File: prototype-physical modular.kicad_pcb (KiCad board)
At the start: 2 copper layers, 100 x 164 mm, 174 parts, among them CON1 BARREL_JACK, CON2 SD_Card, IC1 ATMEGA2560-A, J1 MIDI_IN, J2 MIDI_OUT, P1 POWER, P15 PH, P16 PF, P17 SD_PINS, P18 3VI2C, P2 FTDI, P3 SPI, P4 BUSTI, P5 BUSTO, P7 PA, Q1 BSS138, Q2 BSS138, Q3 BSS138, Q4 BSS138, Q5 BSS138, Q6 BSS138, SW1 SW_PUSH, SW10 SW_PUSH, SW11 SW_PUSH, SW12 SW_PUSH, SW13 SW_PUSH, SW14 SW_PUSH, SW2 ROTARY_ENCODER_SWITCH, SW3 SW_PUSH, SW4 SW_PUSH, SW5 SW_PUSH, SW6 SW_PUSH, SW7 SW_PUSH, SW8 SW_PUSH, SW9 SW_PUSH, U1 NCP1117ST50T3G, U2 6N138, Y1 16MHz

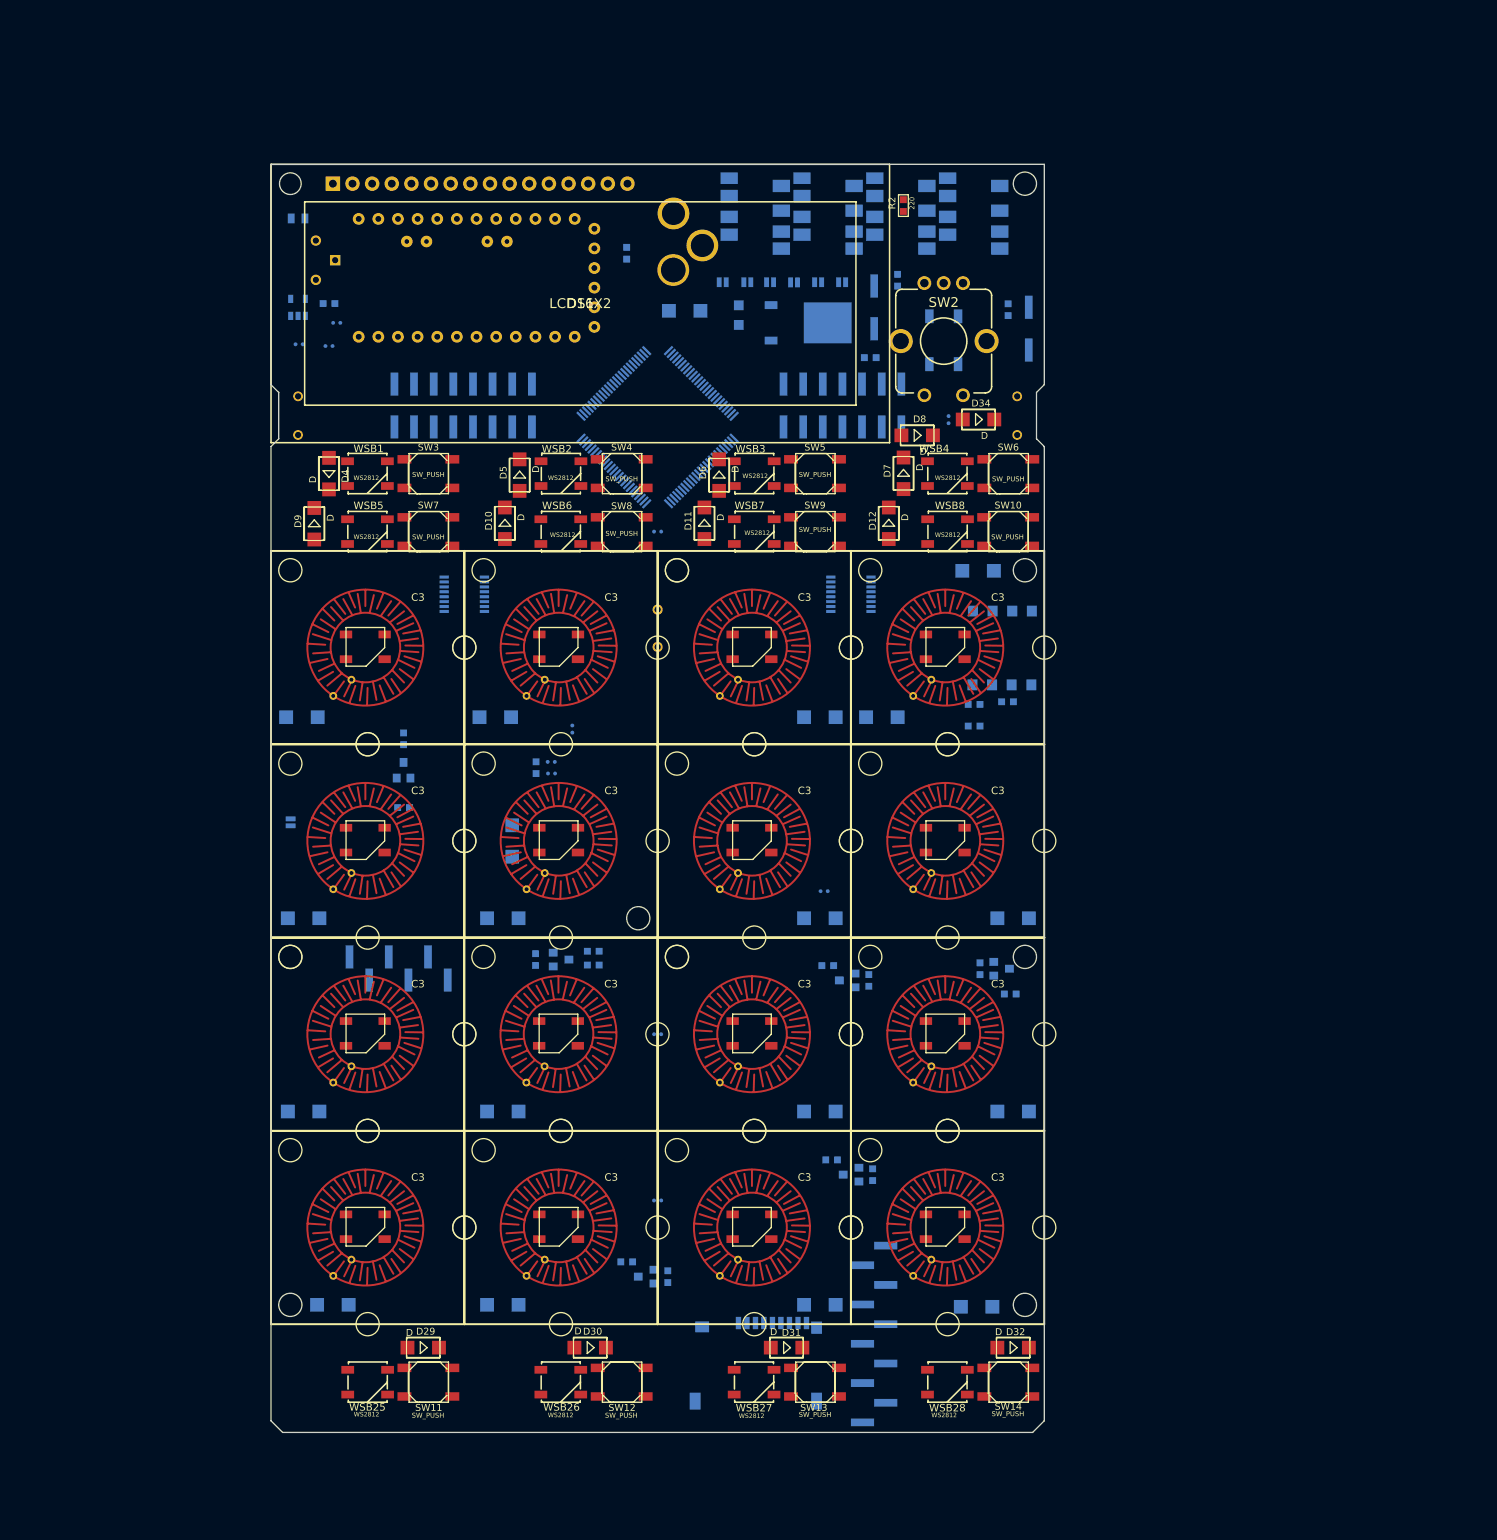
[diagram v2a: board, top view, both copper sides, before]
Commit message: remap pins in prototype tests, and changed TIP and TOP pins in schematic
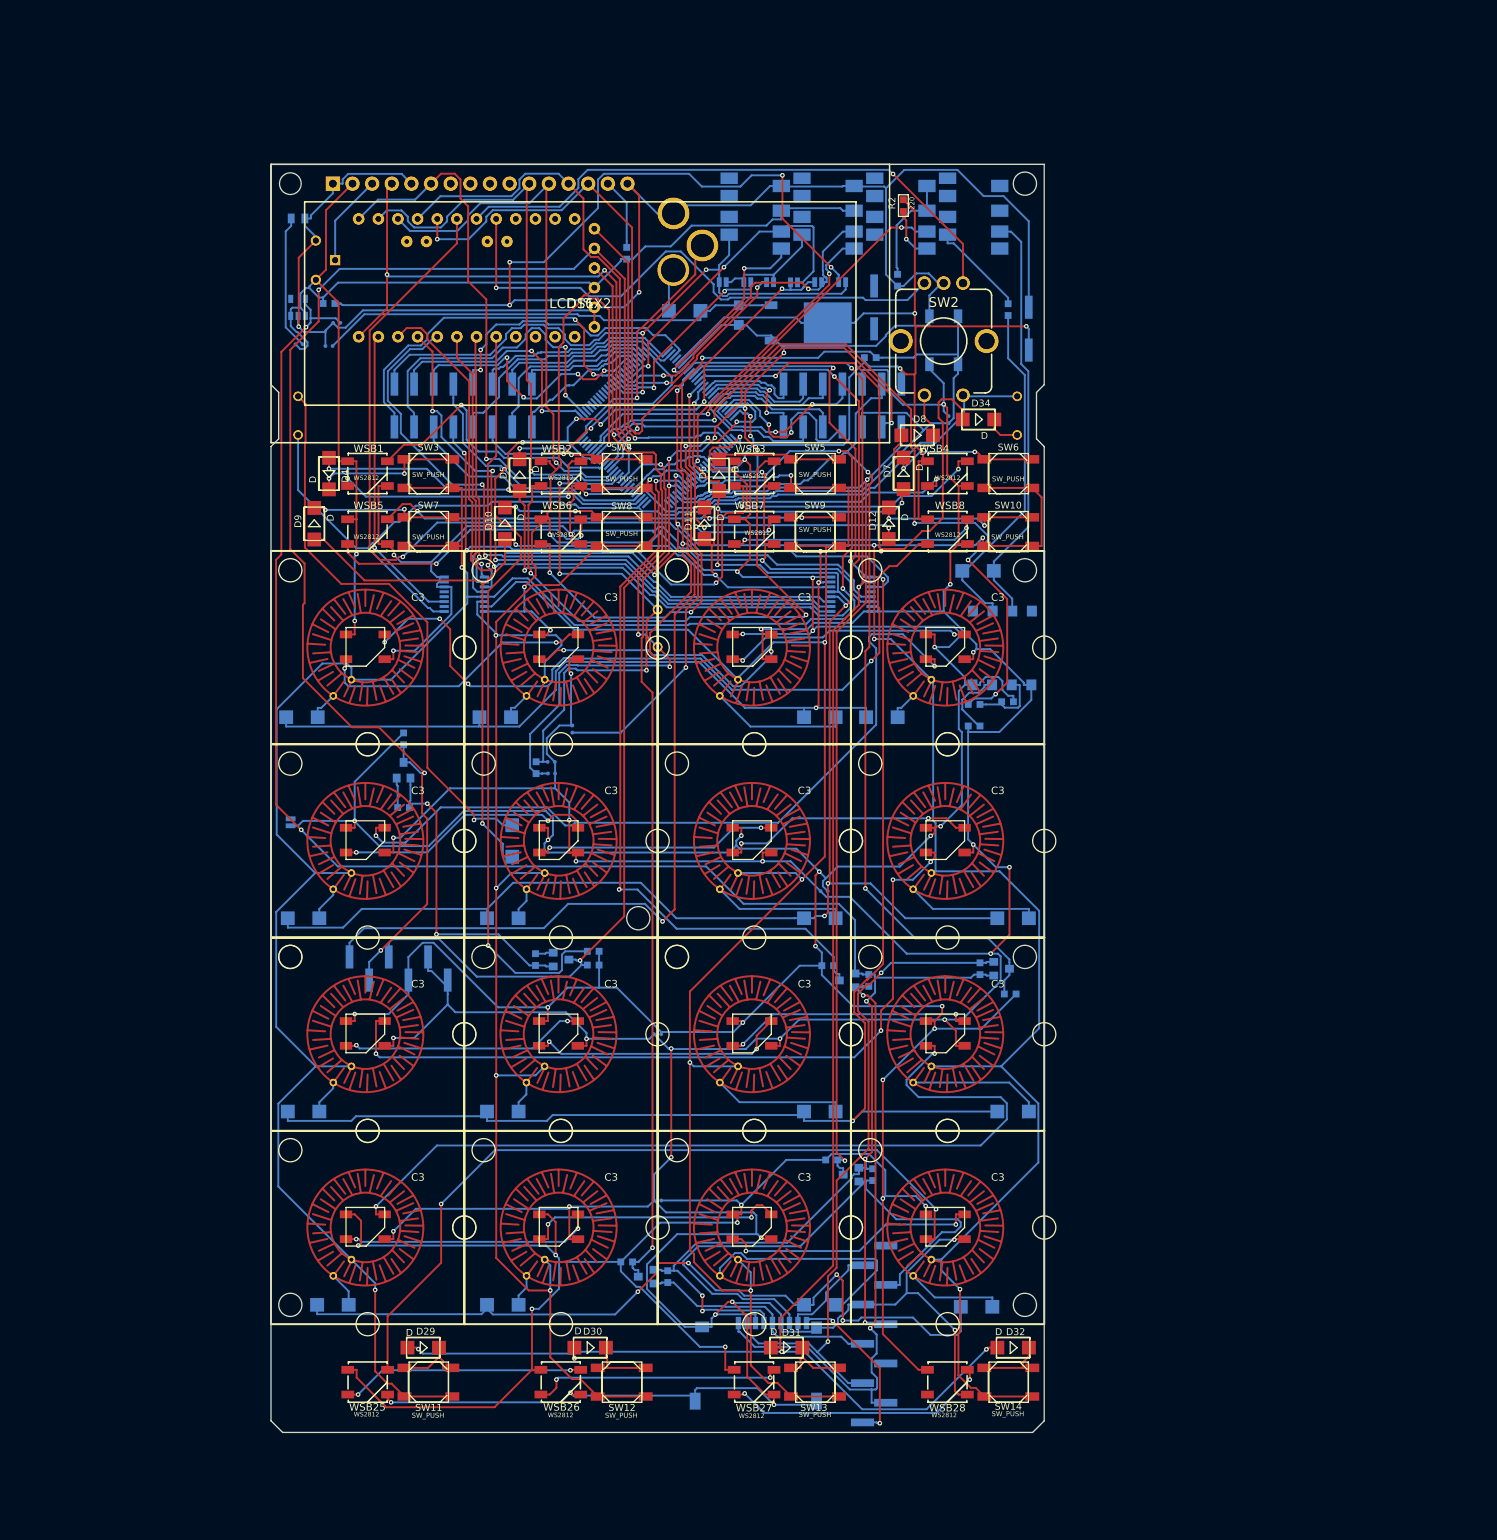
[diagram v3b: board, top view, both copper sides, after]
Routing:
- net GND: track 0.00 -> 1041.3 mm, vias 0 -> 39
- net +5V: track 0.00 -> 1008.6 mm, vias 0 -> 37
- net /MUXAX0: track 0.00 -> 280.3 mm, vias 0 -> 4
- net +3V3: track 0.00 -> 279.2 mm, vias 0 -> 7
- net /RESET: track 0.00 -> 265.7 mm, vias 0 -> 2
- net /MUXAX3: track 0.00 -> 265.0 mm, vias 0 -> 7
- net /MUXBX5: track 0.00 -> 250.4 mm, vias 0 -> 6
- net /MUXBX6: track 0.00 -> 242.3 mm, vias 0 -> 6
- net /MUXAX2: track 0.00 -> 242.1 mm, vias 0 -> 5
- net /MUXBX4: track 0.00 -> 220.3 mm, vias 0 -> 4
- net /MUXAX1: track 0.00 -> 199.3 mm, vias 0 -> 5
- net /MUXBX3: track 0.00 -> 194.2 mm, vias 0 -> 4
- net /MUXBX2: track 0.00 -> 194.0 mm, vias 0 -> 5
- net /TX0: track 0.00 -> 186.9 mm, vias 0 -> 4
- net /MUXBX1: track 0.00 -> 167.3 mm, vias 0 -> 6
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
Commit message: correction of BOM and routing
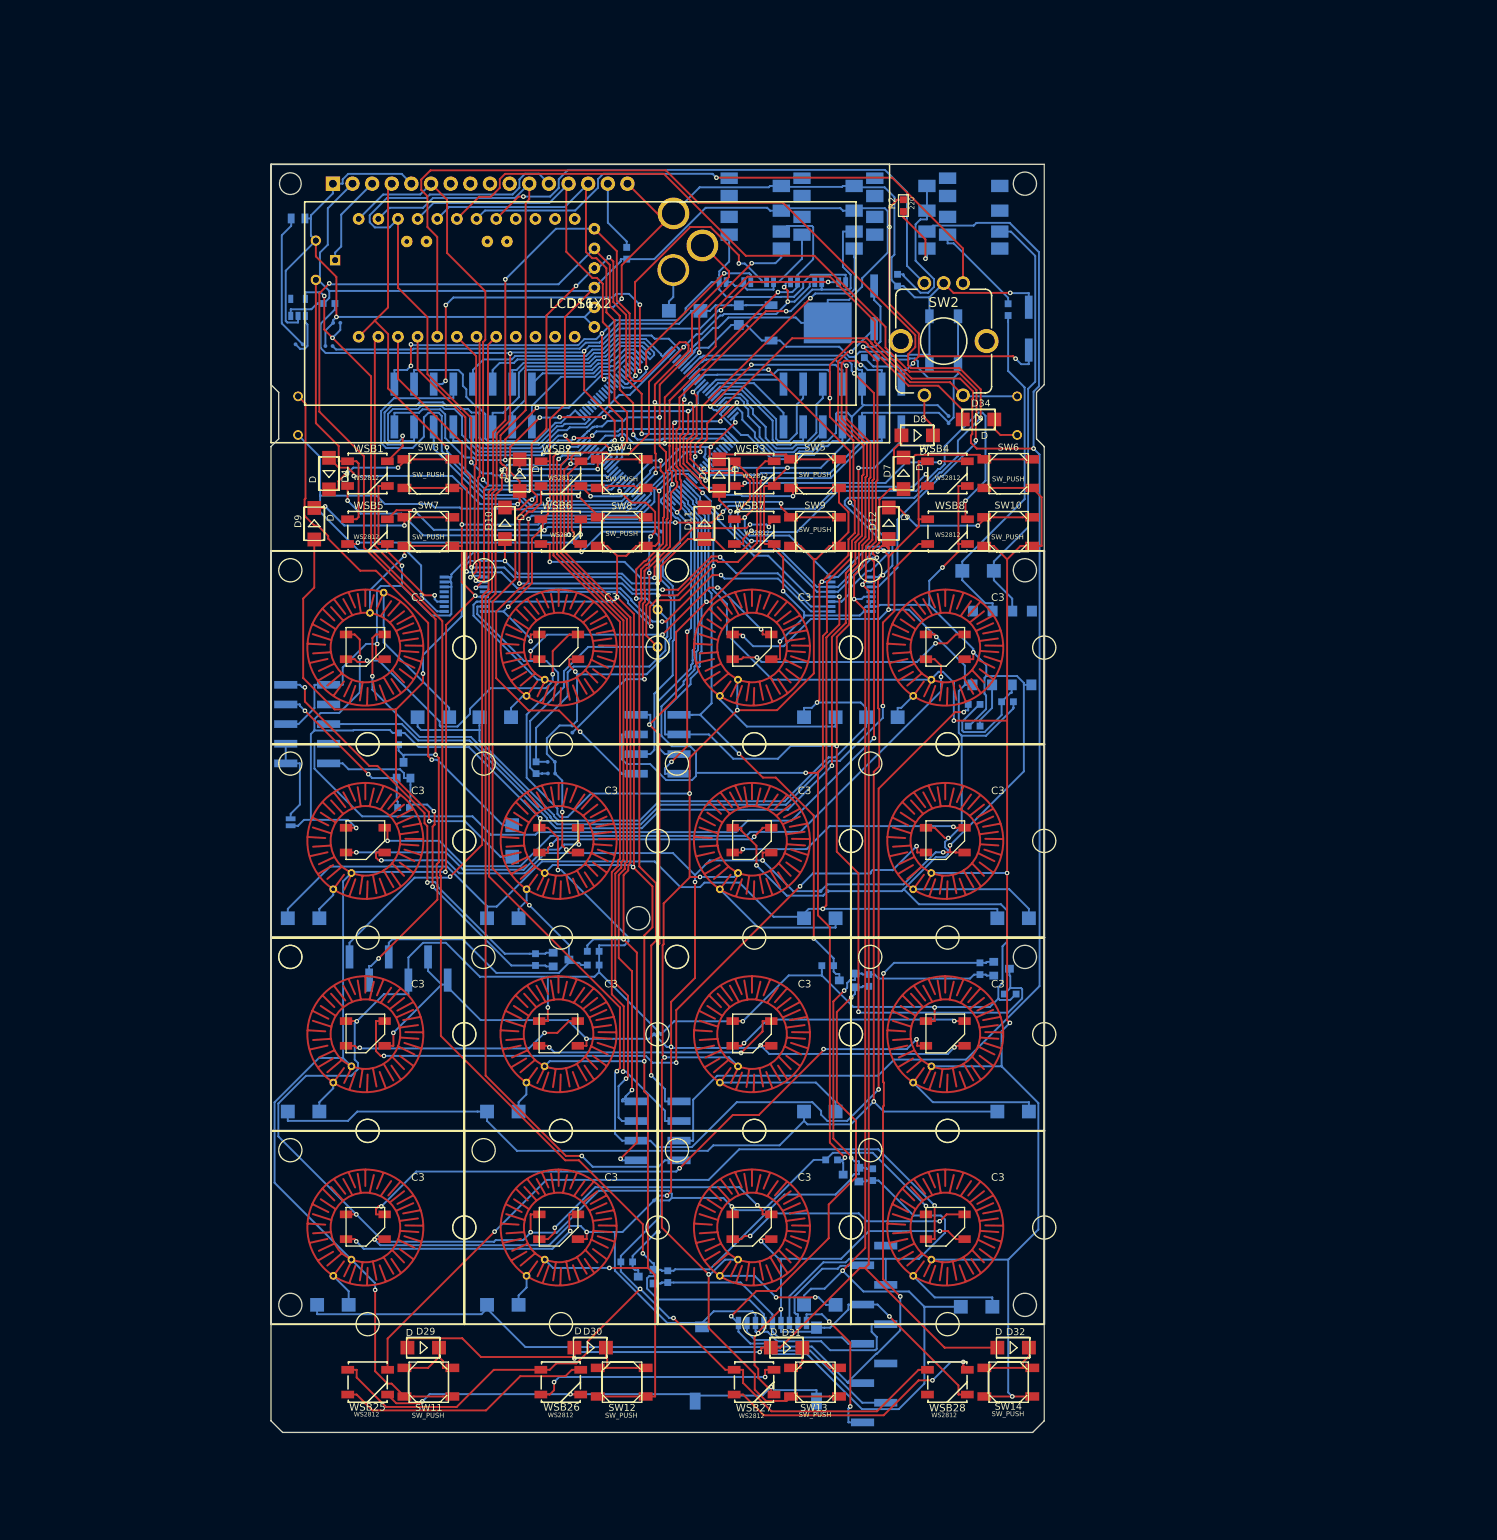
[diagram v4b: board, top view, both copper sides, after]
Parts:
- added P13: PD, Pin_Headers:Pin_Header_Straight_2x04_Pitch2.54mm_SMD, B.Cu at (50.0, 125.0)
- added P19: PIGPIO, lib_fp:Pin_Header_Straight_2x05_Pitch2.54mm_SMD-raspi, B.Cu at (4.67, 72.4)
- added P9: PB, Pin_Headers:Pin_Header_Straight_2x04_Pitch2.54mm_SMD, B.Cu at (50.0, 75.0)
- moved D13 17.0 mm to (21.0, 71.5)
- moved R13 0.64 mm to (16.5, 74.3)
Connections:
- net /RX0 renamed /PI5vRX0
- net /TX0 renamed /PI5vTX0
- IC1 pad 24: Net-(IC1-Pad24) -> /BUS_TI
- IC1 pad 25: Net-(IC1-Pad25) -> /BUS_TO
- IC1 pad 66: /BUS_TO -> Net-(IC1-Pad66)
- IC1 pad 67: /BUS_TI -> Net-(IC1-Pad67)
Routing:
- net /MIDI_OUT_TX: track 56.0 -> 258.8 mm
- net /PI_SDA: track 0.00 -> 148.2 mm, vias 0 -> 2
- net /PI_SCL: track 0.00 -> 135.8 mm, vias 0 -> 2
- net Net-(IC1-Pad48): track 0.00 -> 99.8 mm, vias 0 -> 2
- net /POWER_IS: track 33.3 -> 133.0 mm, vias 1 -> 2
- net /MIDI_RX: track 104.8 -> 202.4 mm
- net Net-(IC1-Pad47): track 0.00 -> 97.5 mm, vias 0 -> 2
- net /SDA: track 121.8 -> 218.8 mm
- net Net-(IC1-Pad49): track 0.00 -> 94.5 mm, vias 0 -> 2
- net /MUXBADDR0: track 86.8 -> 155.8 mm, vias 2 -> 1
- net /MUXAX0: track 280.3 -> 213.8 mm, vias 4 -> 5
- net Net-(IC1-Pad26): track 0.00 -> 61.8 mm, vias 0 -> 2
- net /5VSD_MOSI: track 121.3 -> 182.6 mm, vias 2 -> 3
- net /3vRX0: track 2.34 -> 55.4 mm, vias 0 -> 2
- net /5VSD_MISO: track 128.5 -> 179.1 mm, vias 2 -> 3
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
